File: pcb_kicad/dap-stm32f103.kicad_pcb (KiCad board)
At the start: 2 copper layers, 41.7 x 26.9 mm, 35 parts, among them J1 USB_C_Receptacle_USB2.0, U1 STM32F103CBTx, Y1 SMD-5032_2P_8MHz_20ppm_20pF

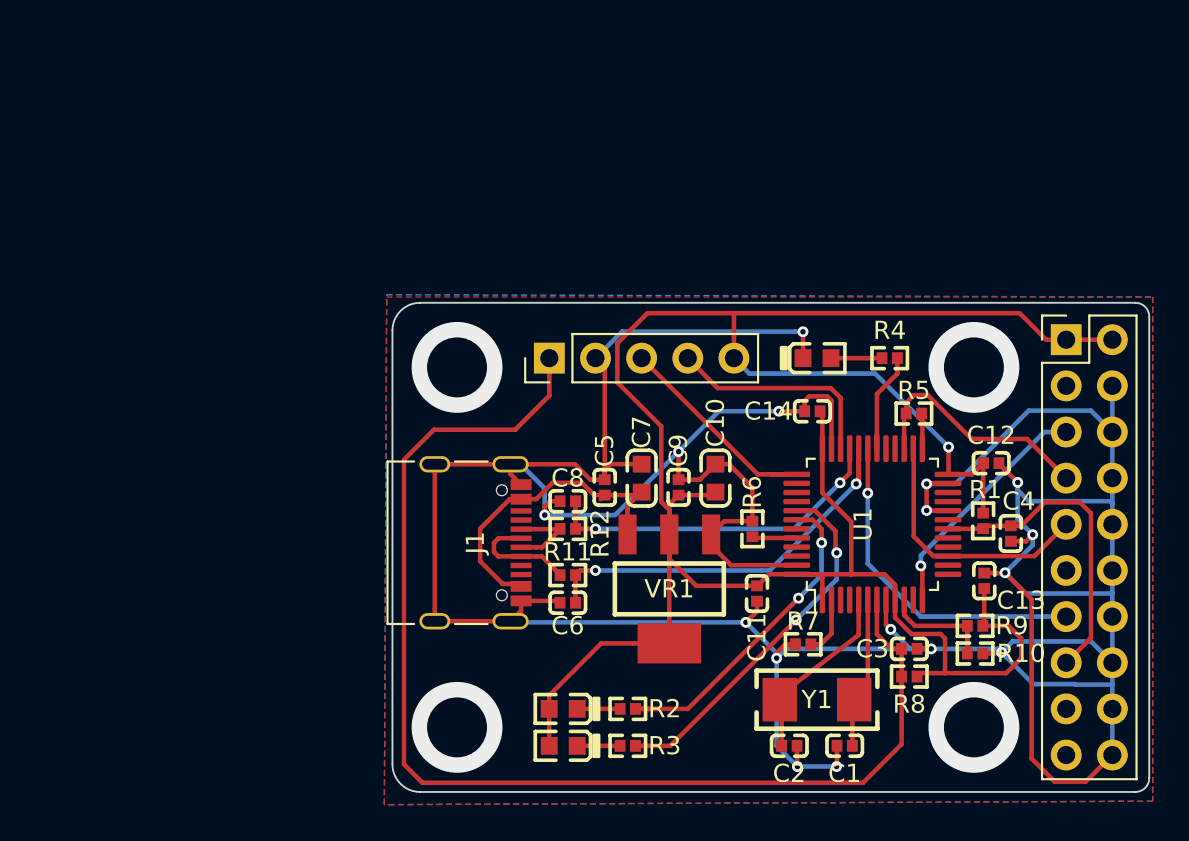
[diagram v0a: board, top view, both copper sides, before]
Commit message: [update] stamp footprint
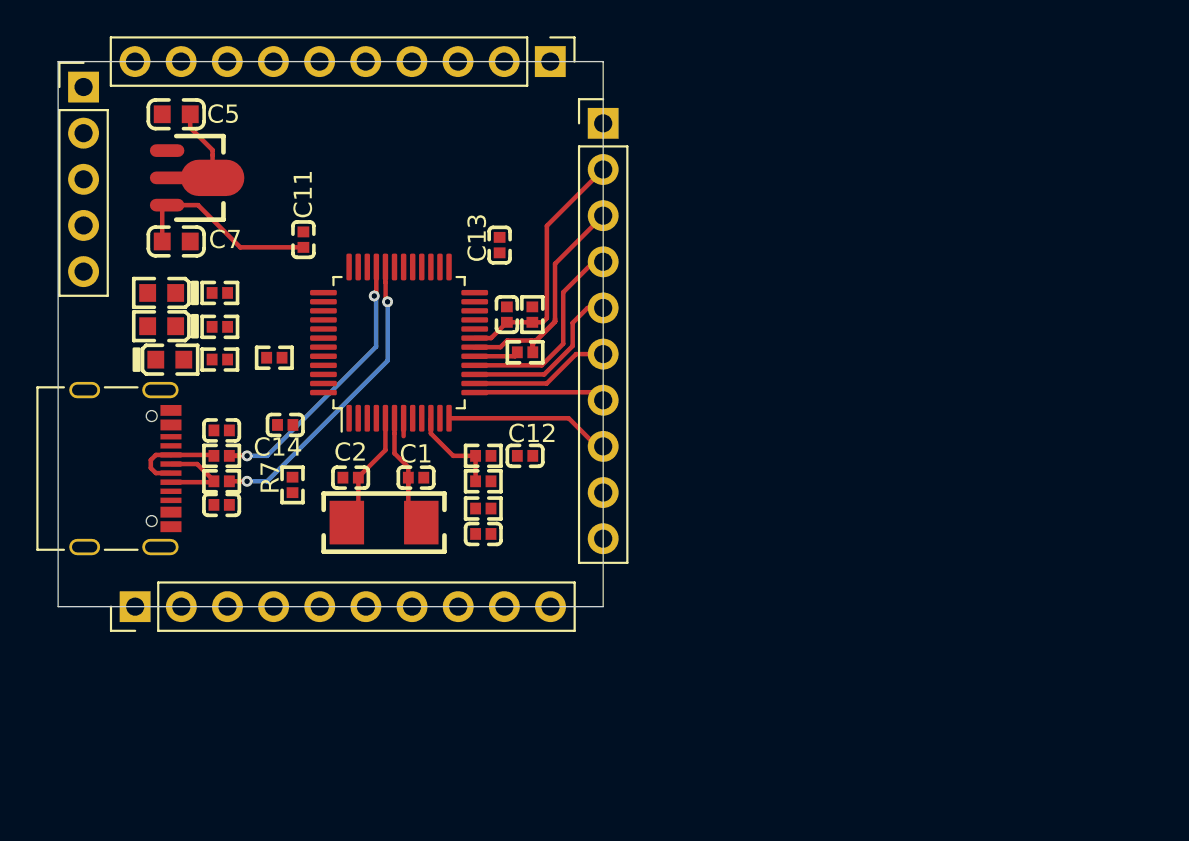
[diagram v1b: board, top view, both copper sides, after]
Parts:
- removed C10: 0603_10uF__106_10%_10V, lc_lib:0603_C
- removed C9: 0402_100nF__104_10%_16V, lc_lib:0402_C
- removed JTAG1: Conn_02x10_Top_Bottom, Connector_PinHeader_2.54mm:PinHeader_2x10_P2.54mm_Vertical
- added J2: Conn_01x10, Connector_PinHeader_2.54mm:PinHeader_1x10_P2.54mm_Vertical, F.Cu at (130.0, 126.3)
- added J3: Conn_01x10, Connector_PinHeader_2.54mm:PinHeader_1x10_P2.54mm_Vertical, F.Cu at (127.1, 122.9)
- added J4: Conn_01x10, Connector_PinHeader_2.54mm:PinHeader_1x10_P2.54mm_Vertical, F.Cu at (104.2, 152.9)
- C5: value 0402_100nF__104_10%_16V -> 0603_10uF__106_10%_10V; footprint lc_lib:0402_C -> lc_lib:0603_C
- VR1: value SOT-223_AMS1117-3.3 -> SOT-89_HT7533-1; footprint lc_lib:SOT-223 -> lc_lib:SOT-89(SOT-89-3)
- moved R4 36.9 mm to (108.9, 139.3)
- moved VR1 35.7 mm to (106.0, 129.3), turned to 180 degrees
- moved D_RED1 35.6 mm to (106.1, 139.3)
- moved R3 33.5 mm to (108.9, 135.6)
- moved D_GREEN1 33.3 mm to (105.7, 135.6)
- moved C13 32.5 mm to (124.3, 133.0)
- moved C11 31.7 mm to (113.5, 132.7), turned to 90 degrees
- moved C5 31.3 mm to (106.5, 125.8), turned to 180 degrees
- moved R2 30.8 mm to (108.9, 137.5)
- moved D_BULE1 30.5 mm to (105.7, 137.4)
- moved C4 30.2 mm to (124.7, 136.8), turned to 90 degrees
- moved IF_SWD1 29.7 mm to (101.4, 124.3), turned to 0 degrees
- moved R7 29.4 mm to (112.9, 146.2), turned to 90 degrees
- moved C14 29.0 mm to (112.5, 142.9)
- moved C7 28.7 mm to (106.5, 132.8), turned to 0 degrees
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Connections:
- C4 pad 1: /TGT_NRESET -> /STAMP_nSRESET
- C5 pad 1: Net-(C5-Pad1) -> +5V
- C7 pad 1: Net-(C5-Pad1) -> +3V3
- J1 pad A4: Net-(C5-Pad1) -> +5V
- J1 pad A5: Net-(J1-PadA5) -> (no net)
- J1 pad A8: Net-(J1-PadA8) -> (no net)
- J1 pad A9: Net-(C5-Pad1) -> +5V
- J1 pad B4: Net-(C5-Pad1) -> +5V
- J1 pad B5: Net-(J1-PadB5) -> (no net)
- J1 pad B8: Net-(J1-PadB8) -> (no net)
- J1 pad B9: Net-(C5-Pad1) -> +5V
- R1 pad 2: /TGT_NRESET -> /STAMP_nSRESET
- R5 pad 1: /TGT_SWDIO -> Net-(R5-Pad1)
- R5 pad 2: Net-(R5-Pad2) -> /STAMP_TMS\SWDIO
- U1 pad 11: Net-(U1-Pad11) -> /PA1
- U1 pad 12: /TGT_RX -> /STAMP_UART_RX
- U1 pad 13: /TGT_TX -> /STAMP_UART_TX
- U1 pad 14: Net-(U1-Pad14) -> /STAMP_TDO
- U1 pad 15: /TGT_SWCLK -> /STAMP_TDI
- U1 pad 16: Net-(U1-Pad16) -> /STAMP_TCLK\SWCLK
- U1 pad 17: Net-(U1-Pad17) -> Net-(R5-Pad1)
- U1 pad 18: /TGT_NRESET -> /STAMP_TMS\SWDIO
- U1 pad 19: Net-(U1-Pad19) -> /STAMP_nSRESET
- U1 pad 21: Net-(U1-Pad21) -> /PB10
- U1 pad 22: Net-(U1-Pad22) -> /PB11
- U1 pad 25: Net-(R5-Pad2) -> /PB12
- U1 pad 26: /TGT_SWCLK -> /PB13
- U1 pad 27: /TGT_SWDIO -> /PB14
- U1 pad 28: Net-(U1-Pad28) -> /PB15
- U1 pad 29: Net-(U1-Pad29) -> /PA8
- U1 pad 3: Net-(U1-Pad3) -> /PC14
- U1 pad 30: /LED_RED -> /PA9
- U1 pad 31: /TGT_SWO -> /PA10
- U1 pad 38: Net-(U1-Pad38) -> /PA15
- U1 pad 39: Net-(U1-Pad39) -> /PB3
- U1 pad 4: Net-(U1-Pad4) -> /PC15
- U1 pad 40: Net-(U1-Pad40) -> /PB4
- U1 pad 43: Net-(U1-Pad43) -> /LED_RED
- U1 pad 45: Net-(U1-Pad45) -> /PB8
- U1 pad 46: Net-(U1-Pad46) -> /PB9
- VR1 pad 2: +3V3 -> +5V
- VR1 pad 3: Net-(C5-Pad1) -> +3V3
- Y1 pad 1: Net-(C2-Pad2) -> Net-(C1-Pad2)
- Y1 pad 2: Net-(C1-Pad2) -> Net-(C2-Pad2)
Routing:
- net GND: track 231.3 -> 0.00 mm, vias 16 -> 0
- net +3V3: track 130.1 -> 10.6 mm, vias 1 -> 0
- net /IF_NRESET: track 65.8 -> 0.98 mm
- net /LED_GREEN: track 20.2 -> 0.00 mm, vias 2 -> 0
- net /LED_BULE: track 18.8 -> 0.00 mm, vias 2 -> 0
- net /TGT_SWO: track 18.5 -> 0.00 mm, vias 1 -> 0
- net Net-(C5-Pad1): track 17.9 -> 0.00 mm
- net /TGT_NRESET: track 17.5 -> 0.00 mm
- net /STAMP_TMS\SWDIO: track 0.00 -> 14.5 mm
- net /TGT_SWCLK: track 14.4 -> 0.00 mm
- net /TGT_SWDIO: track 13.4 -> 0.00 mm
- net /STAMP_nSRESET: track 0.00 -> 13.4 mm
- net /TGT_RX: track 13.3 -> 0.00 mm, vias 1 -> 0
- net /IF_SWCLK: track 12.7 -> 0.00 mm
- net /IF_SWDIO: track 12.1 -> 0.00 mm
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- removed copper zone on B.Cu, net GND
- removed copper zone on F.Cu, net GND
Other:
- board size 41.7 x 26.9 mm -> 30 x 30 mm

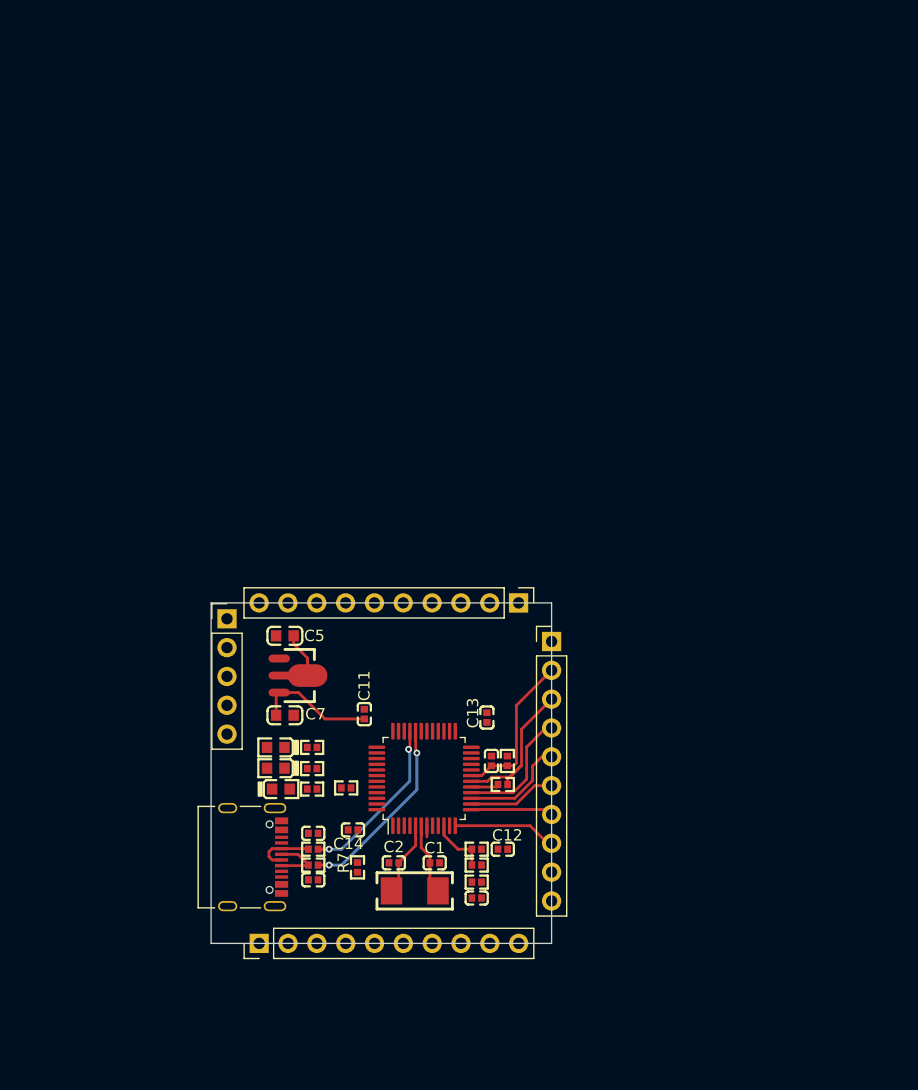
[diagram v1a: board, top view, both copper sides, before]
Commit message: [update] stamp footprint
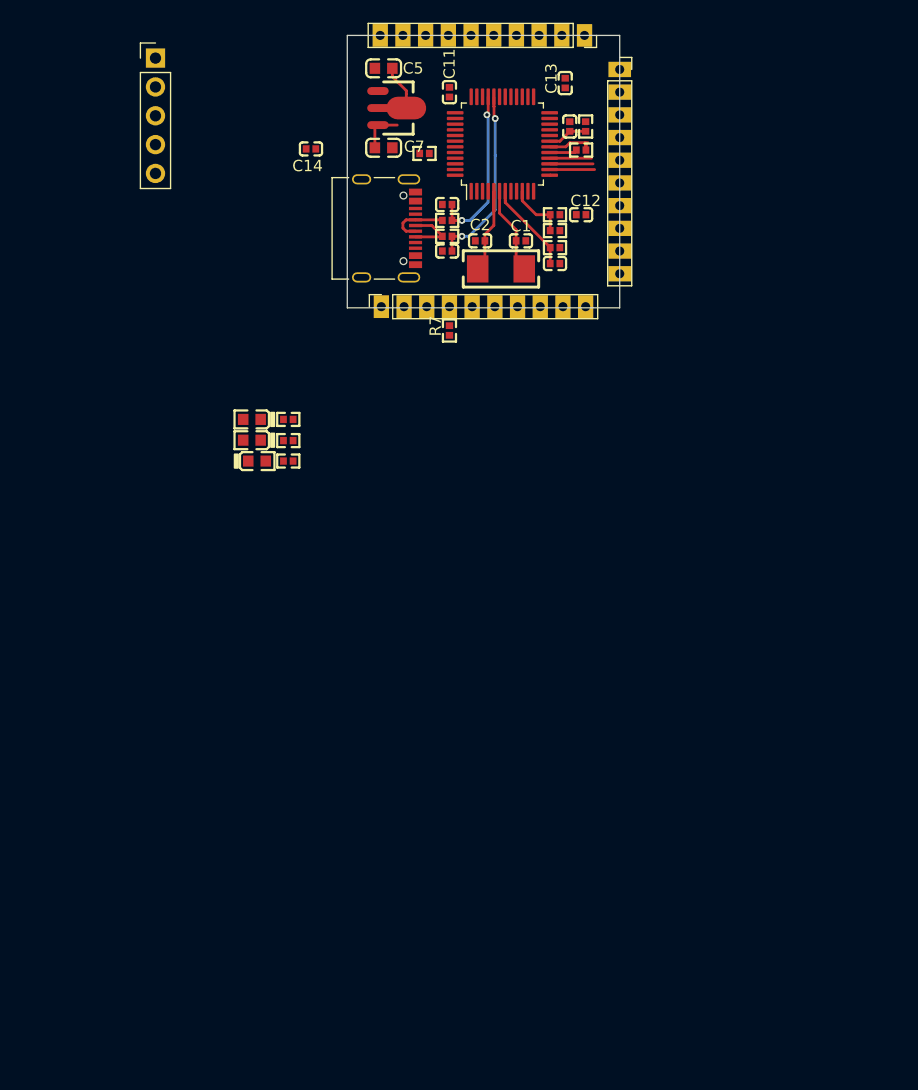
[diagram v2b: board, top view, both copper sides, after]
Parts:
- J2, J3, J4: footprint Connector_PinHeader_2.54mm:PinHeader_1x10_P2.54mm_Vertical -> lc_lib:stamp_2.0mm_1x10
- moved C14 60.1 mm to (108.8, 82.9)
- moved J4 57.1 mm to (115.0, 96.8)
- moved C6 56.6 mm to (120.8, 91.9)
- moved C8 56.6 mm to (120.8, 87.8)
- moved J1 56.6 mm to (115.5, 89.9)
- moved R12 56.6 mm to (120.8, 89.2)
- moved R11 56.6 mm to (120.8, 90.6)
- moved C12 56.3 mm to (132.6, 88.7)
- moved C4 56.3 mm to (131.6, 80.9)
- moved R1 56.3 mm to (133.0, 80.9)
- moved R6 56.3 mm to (118.8, 83.3)
- moved R9 56.3 mm to (130.3, 88.7)
- moved U1 56.3 mm to (125.6, 82.4)
- moved C13 56.3 mm to (131.2, 77.1)
- moved C3 56.3 mm to (130.3, 93.0)
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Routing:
- net /STAMP_nSRESET: track 13.4 -> 3.53 mm
- net /STAMP_TMS\SWDIO: track 14.5 -> 4.68 mm
- net /STAMP_UART_RX: track 8.78 -> 0.00 mm
- net /STAMP_TCLK\SWCLK: track 10.7 -> 3.69 mm
- net /IF_NRESET: track 0.98 -> 8.01 mm
- net +3V3: track 10.6 -> 3.81 mm
- net /STAMP_UART_TX: track 6.77 -> 0.08 mm
- net /STAMP_TDI: track 8.98 -> 3.83 mm
- net /STAMP_TDO: track 7.39 -> 3.96 mm
- net Net-(C2-Pad2): track 6.62 -> 9.19 mm
- net Net-(C1-Pad2): track 6.66 -> 7.74 mm
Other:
- board size 30 x 30 mm -> 24 x 24 mm

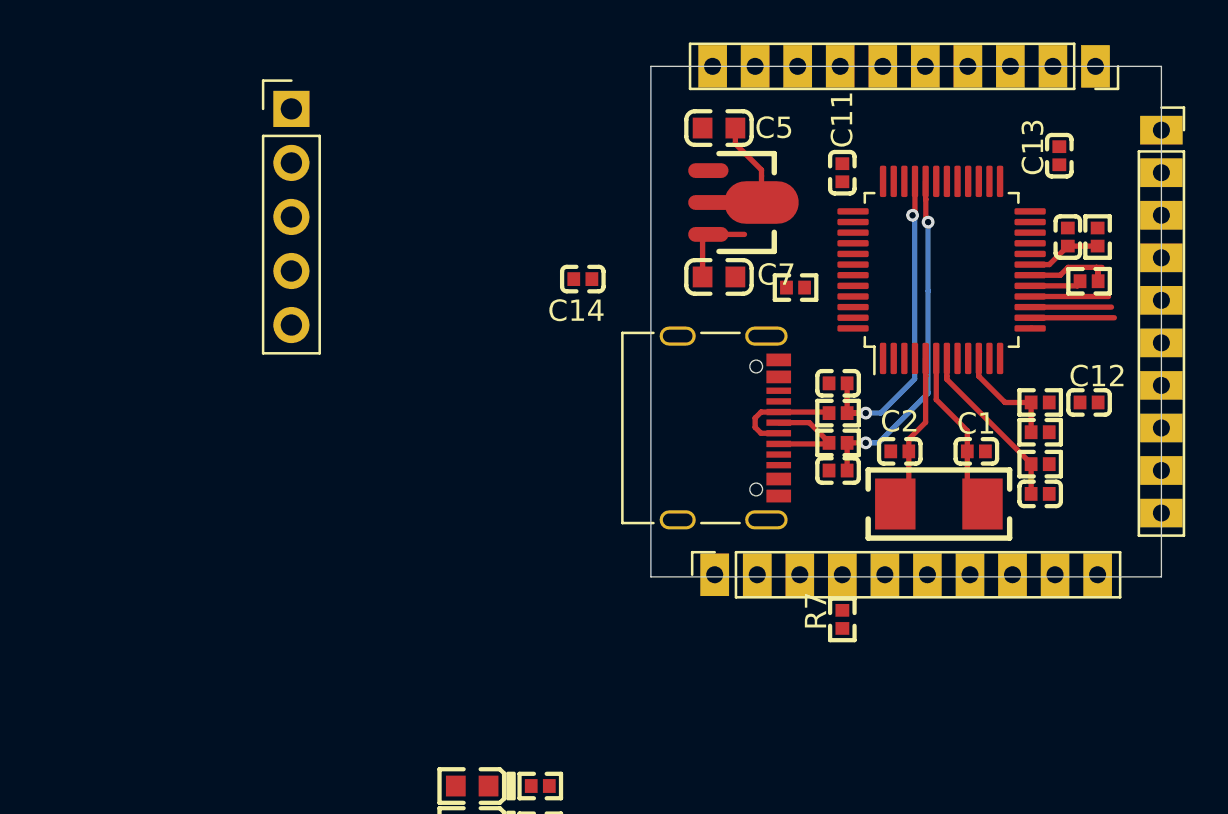
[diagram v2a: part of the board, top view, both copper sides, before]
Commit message: [update] stamp footprint
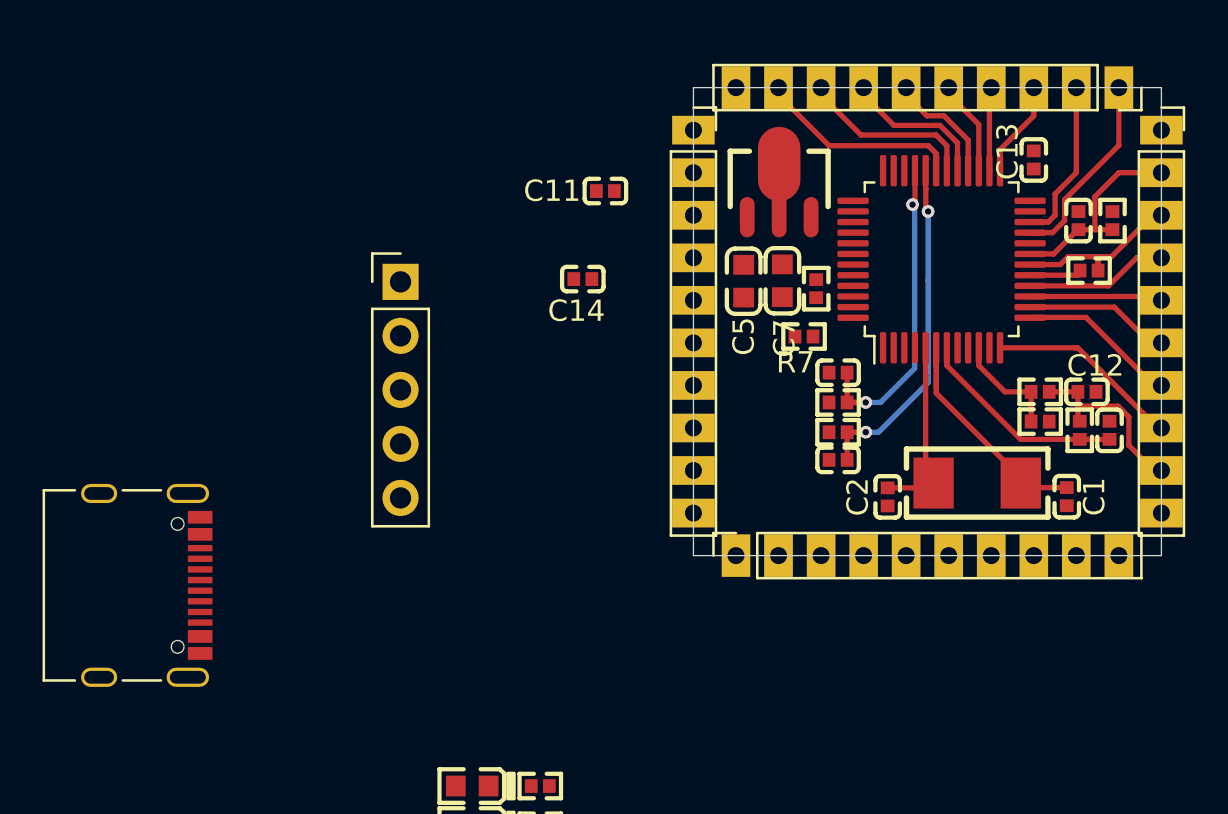
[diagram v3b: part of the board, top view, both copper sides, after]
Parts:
- added J3: Conn_01x10, lc_lib:stamp_2.0mm_1x10, F.Cu at (114.0, 75.9)
- moved J1 28.2 mm to (88.3, 97.3)
- moved R7 13.4 mm to (119.2, 85.6), turned to 180 degrees
- moved C11 11.2 mm to (109.8, 78.7), turned to 180 degrees
- moved IF_SWD1 9.61 mm to (100.2, 83.0)
- moved C5 7.29 mm to (116.3, 83.0), turned to 270 degrees
- moved C1 4.75 mm to (131.5, 93.1), turned to 90 degrees
- moved C3 4.42 mm to (133.5, 90.0), turned to 270 degrees
- moved VR1 3.40 mm to (118.0, 80.0), turned to 270 degrees
- moved C7 2.99 mm to (118.1, 82.9), turned to 270 degrees
- moved R8 2.45 mm to (132.1, 90.0), turned to 270 degrees
- moved C2 2.21 mm to (123.1, 93.1), turned to 90 degrees
- moved Y1 2.05 mm to (127.3, 92.5)
- moved J3 1.49 mm to (134.0, 73.9)
- moved J4 1.35 mm to (116.0, 95.9)
- moved C13 1.22 mm to (130.0, 77.3)
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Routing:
- net /PA10: track 0.00 -> 9.36 mm
- net /STAMP_UART_RX: track 0.00 -> 8.90 mm
- net /PB10: track 0.00 -> 8.81 mm
- net /PA9: track 0.00 -> 8.07 mm
- net /PB11: track 0.00 -> 7.37 mm
- net /STAMP_UART_TX: track 0.08 -> 7.24 mm
- net /PA8: track 0.00 -> 6.65 mm
- net +5V: track 6.41 -> 0.00 mm
- net /STAMP_nSRESET: track 3.53 -> 9.14 mm
- net /PB15: track 0.00 -> 5.23 mm
- net /TGT_USB_D-: track 5.28 -> 0.07 mm
- net /TGT_USB_D+: track 5.16 -> 0.00 mm
- net +3V3: track 3.81 -> 8.38 mm
- net Net-(C1-Pad2): track 7.74 -> 12.2 mm
- net /PB12: track 0.00 -> 4.21 mm
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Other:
- board size 24 x 24 mm -> 22 x 22 mm

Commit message: [done] stamp pcb
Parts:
- removed D_BULE1: 0603_蓝灯, lc_lib:0603_LED_S1
- removed D_GREEN1: 0603_绿灯, lc_lib:0603_LED_S1
- removed D_RED1: 0603_红灯, lc_lib:0603_LED_S1
- removed the J3 at (114.0, 75.9)
- removed R3, R4: 0402_470Ω__4700_1%, lc_lib:0402_R
- IF_SWD1: footprint Connector_PinHeader_2.54mm:PinHeader_1x05_P2.54mm_Vertical -> Connector_PinSocket_1.27mm:PinSocket_1x05_P1.27mm_Vertical
- J1: value USB_C_Receptacle_USB2.0 -> Conn_01x10; footprint Connector_USB:USB_C_Receptacle_Palconn_UTC16-G -> lc_lib:stamp_2.0mm_1x10
- R2: value 0402_470Ω__4700_1% -> 0402_10KΩ__1002_1%
- moved J1 33.4 mm to (114.0, 76.0), turned to 0 degrees
- moved R2 31.4 mm to (133.4, 92.0), turned to 0 degrees
- moved R6 17.0 mm to (133.4, 93.4), turned to 180 degrees
- moved IF_SWD1 16.4 mm to (116.5, 81.6), turned to 180 degrees
- moved R7 13.4 mm to (132.5, 85.7), turned to 135 degrees
- moved VR1 12.2 mm to (119.8, 92.1), turned to 0 degrees
- moved C14 11.6 mm to (119.9, 86.2)
- moved C11 9.57 mm to (119.1, 76.5), turned to 135 degrees
- moved C1 5.22 mm to (127.3, 90.0), turned to 0 degrees
- moved C7 4.82 mm to (117.9, 87.8), turned to 90 degrees
- moved C5 4.81 mm to (116.1, 87.8), turned to 90 degrees
- moved C6 4.25 mm to (123.7, 88.3), turned to 270 degrees
- moved C2 3.68 mm to (125.1, 90.0), turned to 180 degrees
- moved R11 2.37 mm to (122.3, 88.3), turned to 270 degrees
- moved C8 1.61 mm to (119.5, 88.3), turned to 270 degrees
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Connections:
- J2 pad 1: +5V -> GND
- J3 pad 10: (no net) -> GND
- J4 pad 1: /PC14 -> +5V
- J4 pad 10: /TGT_USB_D- -> GND
- J4 pad 2: /PC15 -> /PB8
- J4 pad 3: /PA1 -> /PB9
- J4 pad 4: /PA15 -> /TGT_USB_D-
- J4 pad 5: /PB3 -> /TGT_USB_D+
- J4 pad 6: /PB4 -> /PC14
- J4 pad 7: /PB8 -> /PC15
- J4 pad 8: /PB9 -> /PA1
- J4 pad 9: /TGT_USB_D+ -> +3V3
- R2 pad 1: /LED_BULE -> Net-(R2-Pad1)
- R2 pad 2: Net-(D_BULE1-PadK) -> GND
- U1 pad 20: GND -> Net-(R2-Pad1)
- U1 pad 41: /LED_GREEN -> /PB5
- U1 pad 42: /LED_BULE -> /PB6
- U1 pad 43: /LED_RED -> /PB7
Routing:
- net GND: track 0.00 -> 185.3 mm, vias 0 -> 27
- net +3V3: track 8.38 -> 138.0 mm, vias 0 -> 12
- net /IF_NRESET: track 9.92 -> 36.3 mm, vias 0 -> 1
- net Net-(R6-Pad2): track 0.00 -> 18.6 mm, vias 0 -> 2
- net /PC14: track 0.00 -> 17.9 mm, vias 0 -> 1
- net Net-(R2-Pad1): track 0.00 -> 16.5 mm, vias 0 -> 2
- net /PB7: track 0.00 -> 15.6 mm, vias 0 -> 1
- net /PB8: track 0.00 -> 14.3 mm, vias 0 -> 1
- net /PB6: track 0.00 -> 13.9 mm, vias 0 -> 1
- net /PC15: track 0.00 -> 13.5 mm, vias 0 -> 1
- net /PB5: track 0.00 -> 13.2 mm, vias 0 -> 1
- net /PB9: track 0.00 -> 12.9 mm, vias 0 -> 1
- net /IF_SWDIO: track 0.00 -> 12.1 mm, vias 0 -> 2
- net Net-(R7-Pad2): track 0.00 -> 11.7 mm
- net /PB4: track 0.00 -> 11.2 mm, vias 0 -> 1
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- added copper zone on B.Cu, net GND
- added copper zone on F.Cu, net GND
